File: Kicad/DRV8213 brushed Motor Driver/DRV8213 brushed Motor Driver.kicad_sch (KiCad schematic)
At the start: 26 parts, among them J1 Keystone 3569, J10 1.27mm pin header, J11 1.27mm pin header, J2 Keystone 3579, J3 Keystone 3579, J4 Keystone 3569, J5 Keystone 3569, J6 Keystone 3579, J7 Keystone 3579, J8 Keystone 3569, J9 JST PH 2mm horizontal, U1 DRV8213RTER, U2 LP2981-3.3

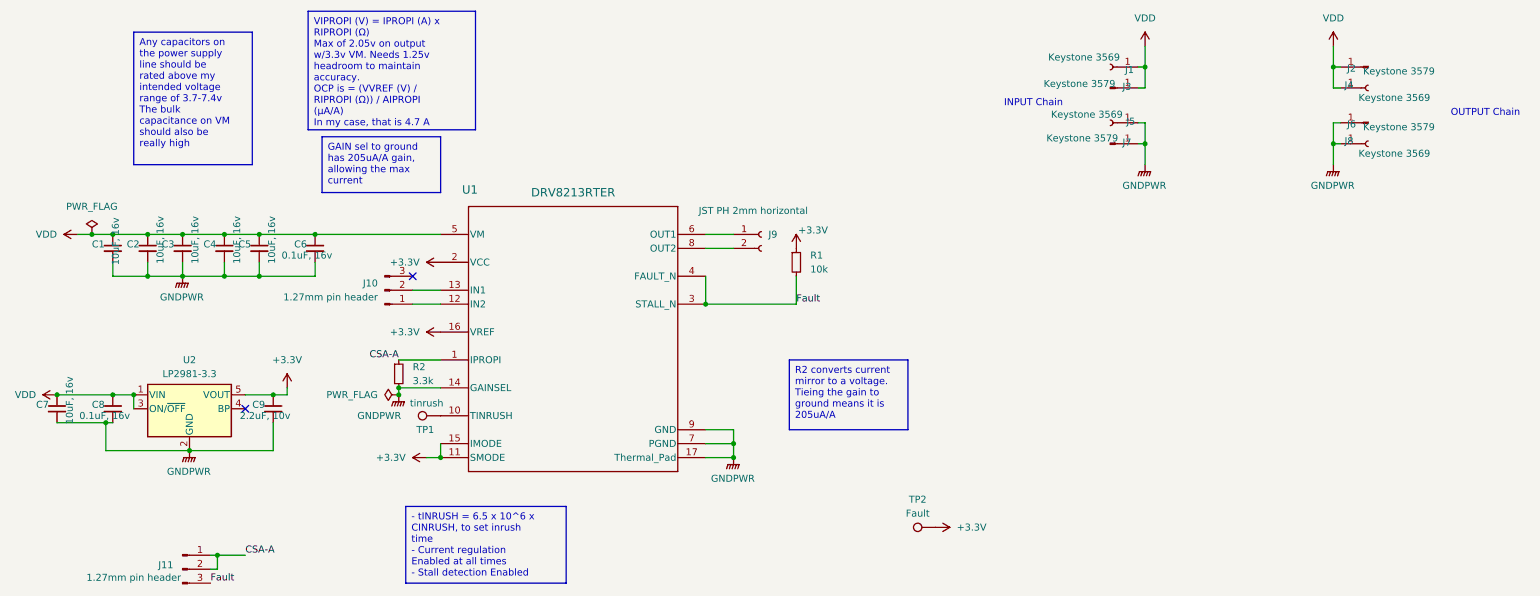
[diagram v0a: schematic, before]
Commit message: Fixed routing of DRV8213 board and updated 3d models
I swapped the current sense and the PWM input headers accidentally! I fixed that now. I also added the proper 3d models and footprints. I exported a 3d model of the board. The last change I made ws cleaning up the inner layers to only be power planes.
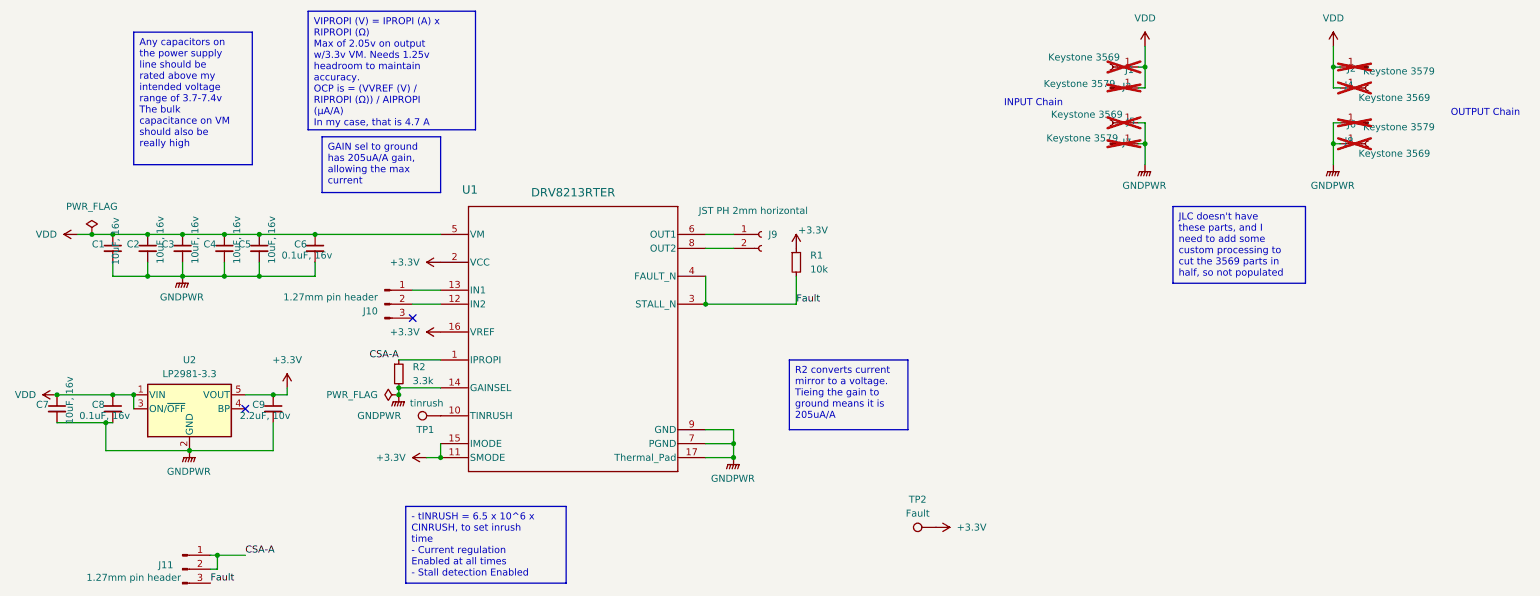
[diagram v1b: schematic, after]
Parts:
- J1, J4, J5, J8: footprint custom_Connector:Keystone_3569 -> custom_Connector:Keystone_3569_half; now not fitted
- J2, J3, J6, J7: now not fitted
- TP1, TP2: now left out of the parts list
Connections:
- net at U1.12 (IN2): now also J10.2 (Pin_2); no longer J10.1 (Pin_1)
- net at U1.13 (IN1): now also J10.1 (Pin_1); no longer J10.2 (Pin_2)
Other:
- moved on the sheet: J10
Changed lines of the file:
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@@
 	)
 	(no_connect
-		(at 82.55 67.31)
+		(at 82.55 74.93)
 	)
 	(wire
@@
 		)
 	)
+	(text_box "JLC doesn't have these parts, and I need to add some custom processing to cut the 3569 parts in half, so not populated"
+		(exclude_from_sim no)
+		(at 220.98 54.61 0)
+		(size 24.13 13.97)
+		(stroke
+			(width 0)
+			(type default)
+		)
+		(fill
+			(type none)
+		)
+		(effects
+			(font
+				(size 1.27 1.27)
+			)
+			(justify left top)
+		)
+	)
 	(text_box "Any capacitors on the power supply line should be rated above my intended voltage range of 3.7-7.4v\nThe bulk capacitance on VM should also be really high"
 		(exclude_from_sim no)
@@
 		(in_bom yes)
 		(on_board yes)
-		(dnp no)
+		(dnp yes)
 		(property "Reference" "J3"
 			(at 212.598 32.766 0)
@@
 		(in_bom yes)
 		(on_board yes)
-		(dnp no)
+		(dnp yes)
 		(property "Reference" "J2"
 			(at 253.492 29.464 0)
@@
 		(in_bom yes)
 		(on_board yes)
-		(dnp no)
+		(dnp yes)
 		(property "Reference" "J7"
 			(at 212.598 42.926 0)
@@
 		(unit 1)
 		(exclude_from_sim no)
-		(in_bom yes)
+		(in_bom no)
 		(on_board yes)
 		(dnp no)
@@
 	(symbol
 		(lib_id "Connector:Conn_01x03_Pin")
-		(at 77.47 69.85 0)
-		(mirror x)
+		(at 77.47 72.39 0)
 		(unit 1)
 		(exclude_from_sim no)
@@
 		(dnp no)
 		(property "Reference" "J10"
-			(at 76.2 68.5799 0)
+			(at 76.2 73.6601 0)
 			(effects
 				(font
@@
 		)
 		(property "Value" "1.27mm pin header"
-			(at 76.2 71.1199 0)
+			(at 76.2 71.1201 0)
 			(effects
 				(font
@@
 		)
 		(property "Footprint" "Connector_PinHeader_1.27mm:PinHeader_1x03_P1.27mm_Horizontal"
-			(at 77.47 69.85 0)
+			(at 77.47 72.39 0)
 			(effects
 				(font
@@
 		)
 		(property "Datasheet" "~"
-			(at 77.47 69.85 0)
+			(at 77.47 72.39 0)
 			(effects
 				(font
@@
 		)
 		(property "Description" "Generic connector, single row, 01x03, script generated"
-			(at 77.47 69.85 0)
+			(at 77.47 72.39 0)
 			(effects
 				(font
@@
 		(in_bom yes)
 		(on_board yes)
-		(dnp no)
+		(dnp yes)
 		(property "Reference" "J1"
 			(at 213.868 29.718 0)
@@
 			)
 		)
-		(property "Footprint" "custom_Connector:Keystone_3569"
+		(property "Footprint" "custom_Connector:Keystone_3569_half"
 			(at 209.55 29.21 0)
 			(effects
@@
 		(in_bom yes)
 		(on_board yes)
-		(dnp no)
+		(dnp yes)
 		(property "Reference" "J6"
 			(at 253.492 39.624 0)
@@
 		(in_bom yes)
 		(on_board yes)
-		(dnp no)
+		(dnp yes)
 		(property "Reference" "J5"
 			(at 214.122 39.116 0)
@@
 			)
 		)
-		(property "Footprint" "custom_Connector:Keystone_3569"
+		(property "Footprint" "custom_Connector:Keystone_3569_half"
 			(at 209.55 39.37 0)
 			(effects
@@
 		(unit 1)
 		(exclude_from_sim no)
-		(in_bom yes)
+		(in_bom no)
 		(on_board yes)
 		(dnp no)
@@
 		(in_bom yes)
 		(on_board yes)
-		(dnp no)
+		(dnp yes)
 		(property "Reference" "J8"
 			(at 252.222 42.672 0)
@@
 			)
 		)
-		(property "Footprint" "custom_Connector:Keystone_3569"
+		(property "Footprint" "custom_Connector:Keystone_3569_half"
 			(at 256.54 43.18 0)
 			(effects
@@
 		(in_bom yes)
 		(on_board yes)
-		(dnp no)
+		(dnp yes)
 		(property "Reference" "J4"
 			(at 252.222 32.512 0)
@@
 			)
 		)
-		(property "Footprint" "custom_Connector:Keystone_3569"
+		(property "Footprint" "custom_Connector:Keystone_3569_half"
 			(at 256.54 33.02 0)
 			(effects

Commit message: Added LCSC part numbers, DNP attr, and exported Gerbers
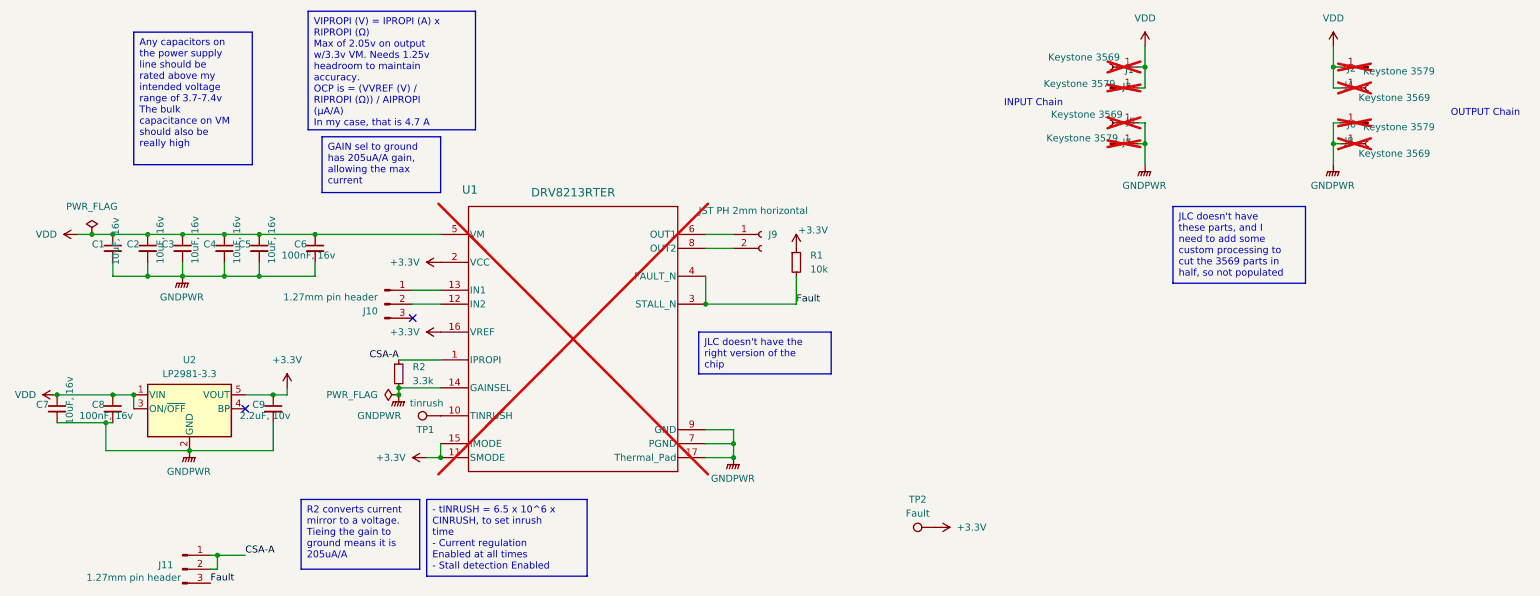
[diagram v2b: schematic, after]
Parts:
- C1, C2, C3, C4, C5, C7: LCSC (none) -> C96446
- C6, C8: value 0.1uF, 16v -> 100nF, 16v; LCSC (none) -> C1525
- C9: LCSC (none) -> C12530
- J9: LCSC (none) -> C295747
- R1: LCSC (none) -> C25744
- R2: LCSC (none) -> C25890
- U1: now not fitted
- U2: LCSC (none) -> C129997
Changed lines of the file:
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@@
 	(text_box "R2 converts current mirror to a voltage. Tieing the gain to ground means it is 205uA/A"
 		(exclude_from_sim no)
-		(at 151.13 82.55 0)
+		(at 62.23 107.95 0)
 		(size 21.59 12.7)
 		(stroke
@@
 	(text_box "- tINRUSH = 6.5 x 10^6 x CINRUSH, to set inrush time\n- Current regulation Enabled at all times\n- Stall detection Enabled"
 		(exclude_from_sim no)
-		(at 81.28 109.22 0)
+		(at 85.09 107.95 0)
 		(size 29.21 13.97)
 		(stroke
@@
 		(at 220.98 54.61 0)
 		(size 24.13 13.97)
+		(stroke
+			(width 0)
+			(type default)
+		)
+		(fill
+			(type none)
+		)
+		(effects
+			(font
+				(size 1.27 1.27)
+			)
+			(justify left top)
+		)
+	)
+	(text_box "JLC doesn't have the right version of the chip"
+		(exclude_from_sim no)
+		(at 134.62 77.47 0)
+		(size 24.13 7.62)
 		(stroke
 			(width 0)
@@
 			)
 		)
+		(property "LCSC" "C25890"
+			(at 82.55 83.8199 0)
+			(effects
+				(font
+					(size 1.27 1.27)
+				)
+				(hide yes)
+			)
+		)
 		(pin "2"
 		)
@@
 			)
 		)
+		(property "LCSC" "C96446"
+			(at 13.97 90.678 0)
+			(effects
+				(font
+					(size 1.27 1.27)
+				)
+				(hide yes)
+			)
+		)
 		(pin "1"
 		)
@@
 		(property "Description" "Unpolarized capacitor, small symbol"
 			(at 40.64 62.23 0)
+			(effects
+				(font
+					(size 1.27 1.27)
+				)
+				(hide yes)
+			)
+		)
+		(property "LCSC" "C96446"
+			(at 36.83 61.468 0)
 			(effects
 				(font
@@
 			)
 		)
+		(property "LCSC" "C96446"
+			(at 30.48 61.468 0)
+			(effects
+				(font
+					(size 1.27 1.27)
+				)
+				(hide yes)
+			)
+		)
 		(pin "1"
 		)
@@
 		(in_bom yes)
 		(on_board yes)
-		(dnp no)
+		(dnp yes)
 		(property "Reference" "U1"
 			(at 92.964 51.562 0)
@@
 		(property "Description" "Unpolarized capacitor, small symbol"
 			(at 48.26 62.23 0)
+			(effects
+				(font
+					(size 1.27 1.27)
+				)
+				(hide yes)
+			)
+		)
+		(property "LCSC" "C96446"
+			(at 44.45 61.468 0)
 			(effects
 				(font
@@
 			)
 		)
+		(property "LCSC" "C12530"
+			(at 53.34 90.678 0)
+			(effects
+				(font
+					(size 1.27 1.27)
+				)
+				(hide yes)
+			)
+		)
 		(pin "1"
 		)
@@
 			)
 		)
+		(property "LCSC" "C96446"
+			(at 24.13 61.468 0)
+			(effects
+				(font
+					(size 1.27 1.27)
+				)
+				(hide yes)
+			)
+		)
 		(pin "1"
 		)
@@
 			)
 		)
+		(property "LCSC" "C96446"
+			(at 50.8 61.468 0)
+			(effects
+				(font
+					(size 1.27 1.27)
+				)
+				(hide yes)
+			)
+		)
 		(pin "1"
 		)
@@
 			)
 		)
-		(property "Value" "0.1uF, 16v"
+		(property "Value" "100nF, 16v"
 			(at 21.844 92.71 0)
 			(effects
@@
 			)
 		)
+		(property "LCSC" "C1525"
+			(at 24.13 90.678 0)
+			(effects
+				(font
+					(size 1.27 1.27)
+				)
+				(hide yes)
+			)
+		)
 		(pin "1"
 		)
@@
 		(property "Description" "Generic connector, single row, 01x02, script generated"
 			(at 146.05 59.69 0)
+			(effects
+				(font
+					(size 1.27 1.27)
+				)
+				(hide yes)
+			)
+		)
+		(property "LCSC" "C295747"
+			(at 147.32 59.6899 0)
 			(effects
 				(font
@@
 			)
 		)
-		(property "Value" "0.1uF, 16v"
+		(property "Value" "100nF, 16v"
 			(at 58.674 63.5 0)
 			(effects
@@
 		(property "Description" "Unpolarized capacitor, small symbol"
 			(at 64.77 62.23 0)
+			(effects
+				(font
+					(size 1.27 1.27)
+				)
+				(hide yes)
+			)
+		)
+		(property "LCSC" "C1525"
+			(at 60.96 61.468 0)
 			(effects
 				(font
@@
 			)
 		)
+		(property "LCSC" "C129997"
+			(at 41.91 82.55 0)
+			(effects
+				(font
+					(size 1.27 1.27)
+				)
+				(hide yes)
+			)
+		)
 		(pin "5"
 		)
@@
 			(effects
 				(font
+					(size 1.27 1.27)
+				)
+				(hide yes)
+			)
+		)
+		(property "LCSC" "C25744"
+			(at 154.94 63.4999 0)
+			(effects
+				(font
